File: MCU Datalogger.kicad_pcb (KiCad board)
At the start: 2 copper layers, 29 parts, among them J1 Conn_01x04_Pin, J2 Conn_01x09_Pin, J3 Conn_01x04_Pin, J4 Conn_02x03_Odd_Even, U1 DS1337S+, U2 24LC1025, U3 24LC1025, U4 ATMEGA328P-AU, Y1 32.768 KHz, Y2 16 MHz

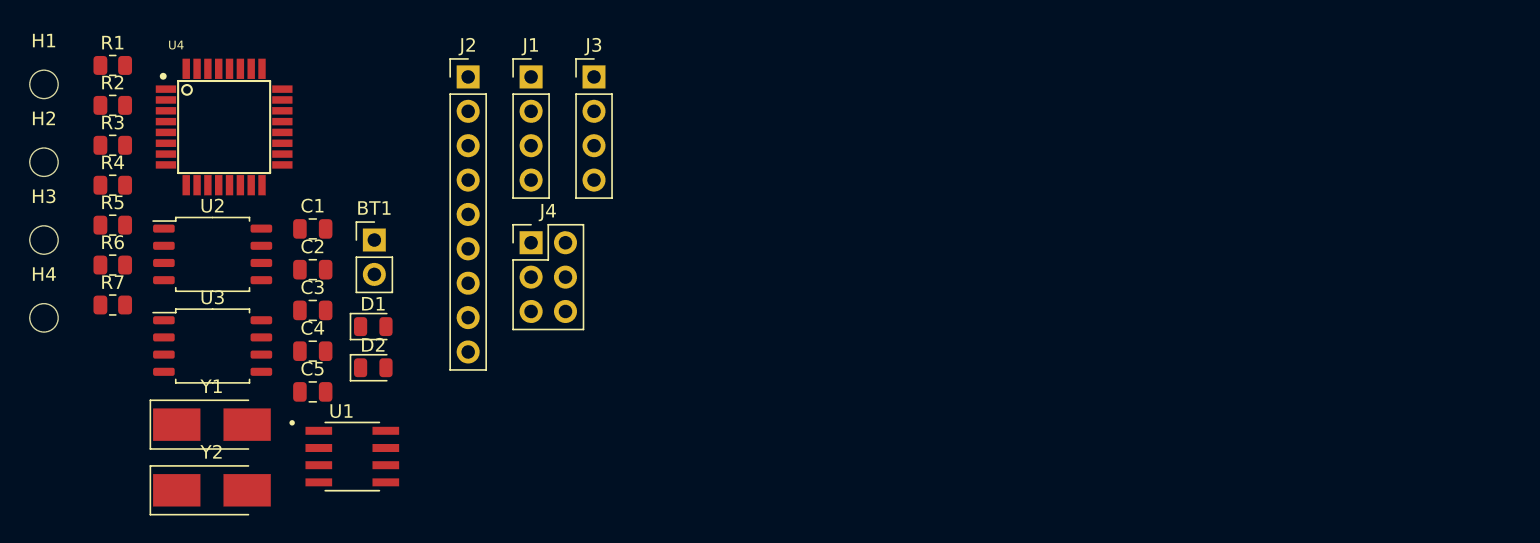
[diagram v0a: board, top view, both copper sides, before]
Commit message: Completed placement of footprints.
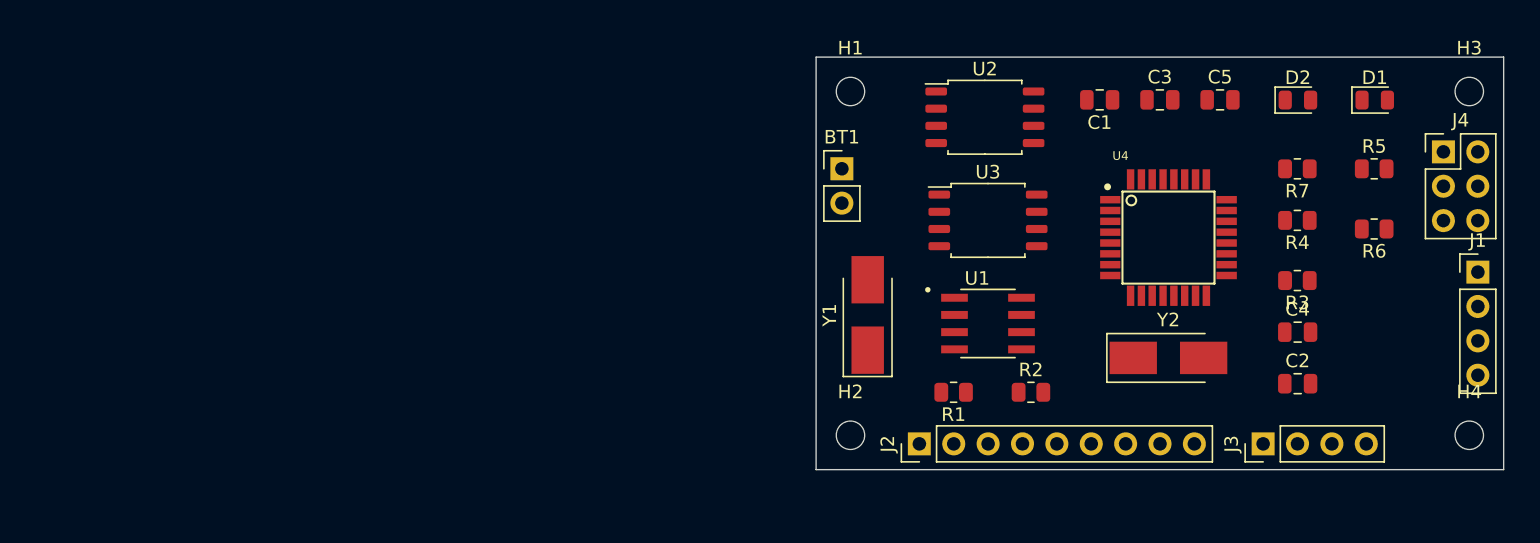
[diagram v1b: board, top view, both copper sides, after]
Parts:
- moved H3 105.9 mm to (165.7, 67.3)
- moved H4 105.7 mm to (165.7, 92.7)
- moved R5 93.3 mm to (158.7, 73.0)
- moved R6 93.2 mm to (158.7, 77.5), turned to 180 degrees
- moved R7 88.1 mm to (153.0, 73.0), turned to 180 degrees
- moved R3 88.1 mm to (153.0, 81.3), turned to 180 degrees
- moved R4 87.6 mm to (153.0, 76.8), turned to 180 degrees
- moved D1 75.9 mm to (158.8, 67.9)
- moved C2 73.3 mm to (153.1, 88.9)
- moved C4 72.8 mm to (153.1, 85.1)
- moved J1 71.4 mm to (166.4, 80.7)
- moved Y2 71.3 mm to (143.5, 87.0)
- moved D2 71.1 mm to (153.1, 67.9)
- moved R2 71.1 mm to (133.3, 89.5)
- moved C5 70.4 mm to (147.3, 67.9)
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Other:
- board outline added: 50.8 x 30.5 mm

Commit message: Refined and completed outline
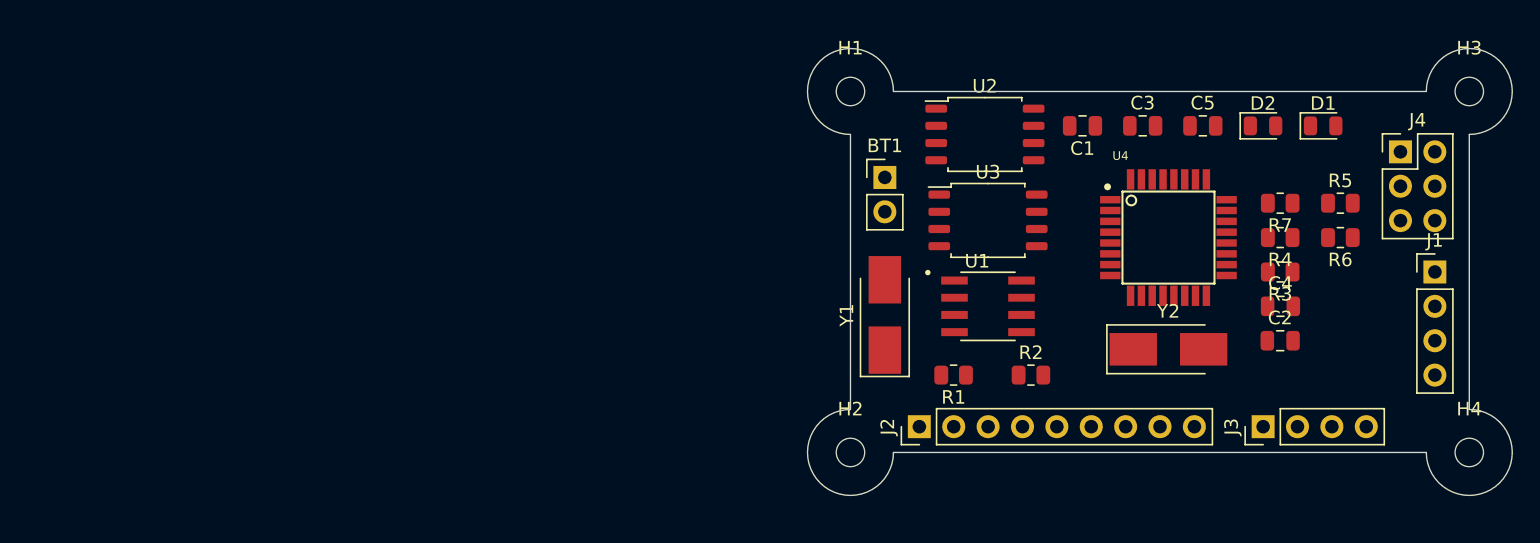
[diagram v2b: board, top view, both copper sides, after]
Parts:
- moved D1 4.26 mm to (154.9, 69.8)
- moved R5 3.56 mm to (156.2, 75.6)
- moved C2 3.43 mm to (151.8, 85.7)
- moved BT1 3.24 mm to (122.6, 73.7)
- moved D2 3.21 mm to (150.5, 69.8)
- moved J1 3.18 mm to (163.2, 80.6)
- moved J4 3.17 mm to (160.7, 71.8)
- moved R7 2.84 mm to (151.8, 75.6)
- moved R6 2.58 mm to (156.2, 78.1)
- moved C1 2.30 mm to (137.2, 69.8)
- moved C3 2.30 mm to (141.6, 69.8)
- moved C5 2.30 mm to (146.1, 69.8)
- moved C4 2.29 mm to (151.8, 83.2)
- moved R4 1.80 mm to (151.8, 78.1)
- moved R3 1.42 mm to (151.8, 80.6)
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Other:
- board size 50.8 x 30.5 mm -> 52.1 x 33 mm

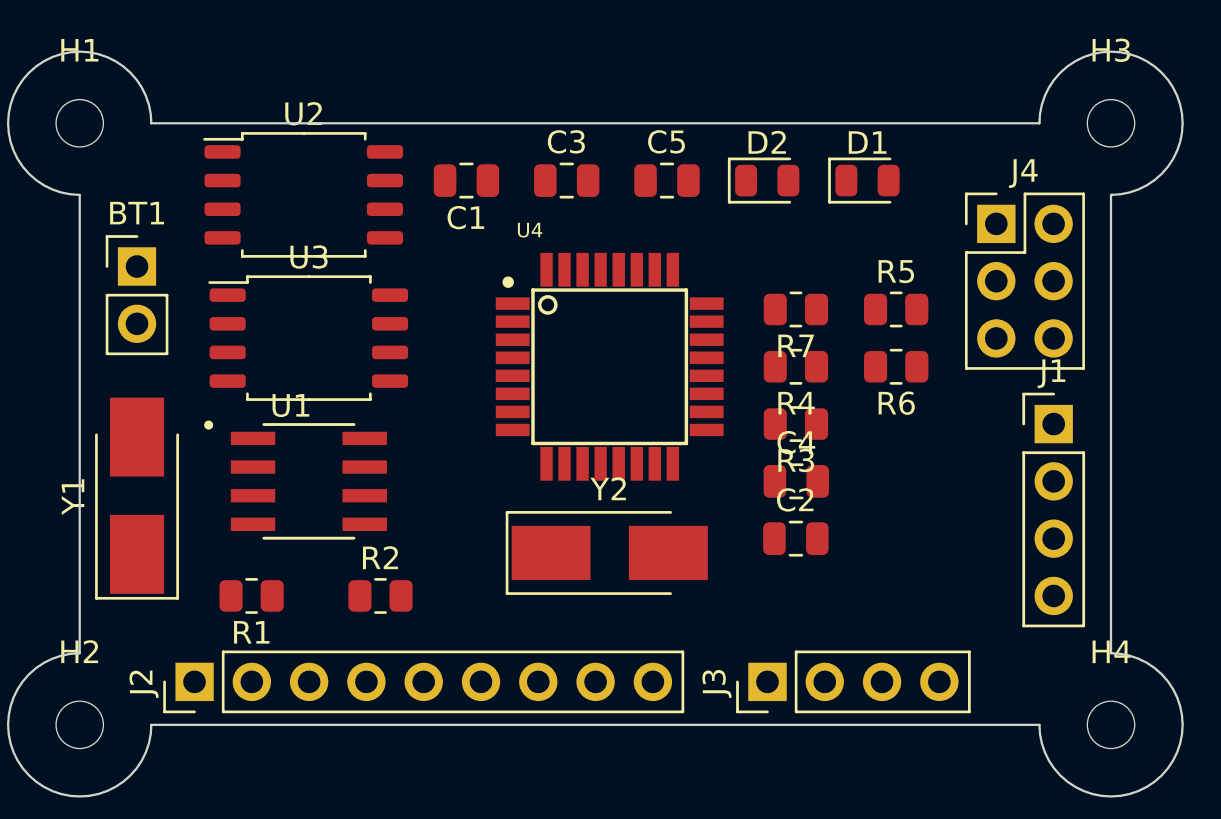
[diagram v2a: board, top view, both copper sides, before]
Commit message: Routing sans GND Vcc complete.
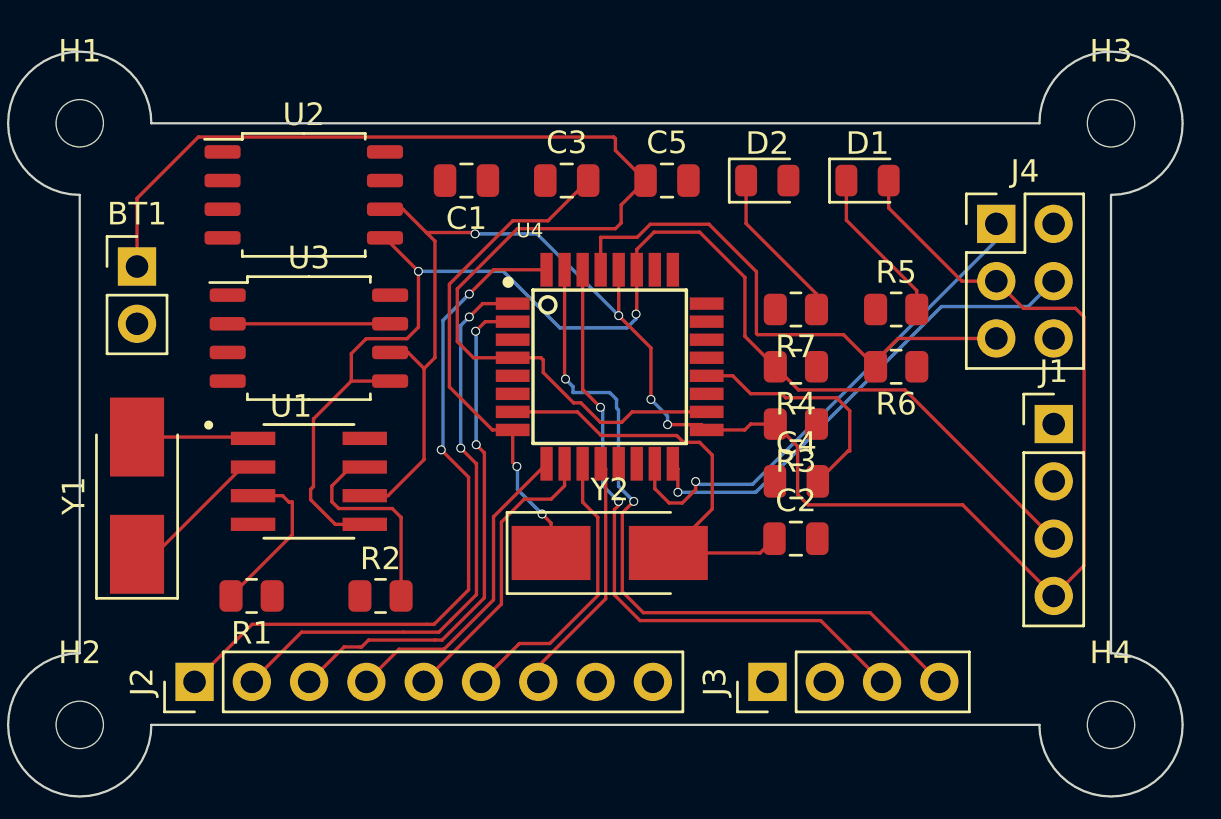
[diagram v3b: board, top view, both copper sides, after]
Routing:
- net /SCK: track 0.00 -> 82.8 mm, vias 0 -> 4
- net /SDA: track 0.00 -> 59.7 mm, vias 0 -> 2
- net Net-(BT1-+): track 0.00 -> 54.0 mm
- net /TX: track 0.00 -> 32.4 mm, vias 0 -> 2
- net /D2: track 0.00 -> 31.8 mm, vias 0 -> 2
- net /RX: track 0.00 -> 28.6 mm, vias 0 -> 2
- net /D3: track 0.00 -> 26.5 mm, vias 0 -> 2
- net /RESET: track 0.00 -> 24.1 mm
- net /D4: track 0.00 -> 23.1 mm, vias 0 -> 2
- net /MOSI: track 0.00 -> 22.4 mm, vias 0 -> 1
- net Net-(U4-PB7): track 0.00 -> 22.4 mm, vias 0 -> 2
- net /MISO: track 0.00 -> 21.9 mm, vias 0 -> 1
- net Net-(U4-PB6): track 0.00 -> 19.8 mm
- net /D5: track 0.00 -> 14.1 mm
- net /D6: track 0.00 -> 13.0 mm
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
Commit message: Completed wiring. Many improvements pending.
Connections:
- BT1 pad 1: Net-(BT1-+) -> /Vcc
- C5 pad 1: Net-(BT1-+) -> /Vcc
- D2 pad 2: Net-(BT1-+) -> /Vcc
- U4 pad 18: Net-(BT1-+) -> /Vcc
- U4 pad 4: Net-(BT1-+) -> /Vcc
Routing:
- net /Vcc: track 0.00 -> 97.7 mm, vias 0 -> 8
- net Net-(BT1-+): track 54.0 -> 0.00 mm
- net GND: track 0.00 -> 37.7 mm, vias 0 -> 10
- net Net-(U4-AREF): track 10.8 -> 12.5 mm
- net /TX: track 32.4 -> 31.5 mm
- net /SDA: track 59.7 -> 59.0 mm
- added copper zone on F.Cu, net /Vcc
- added copper zone on B.Cu, net GND

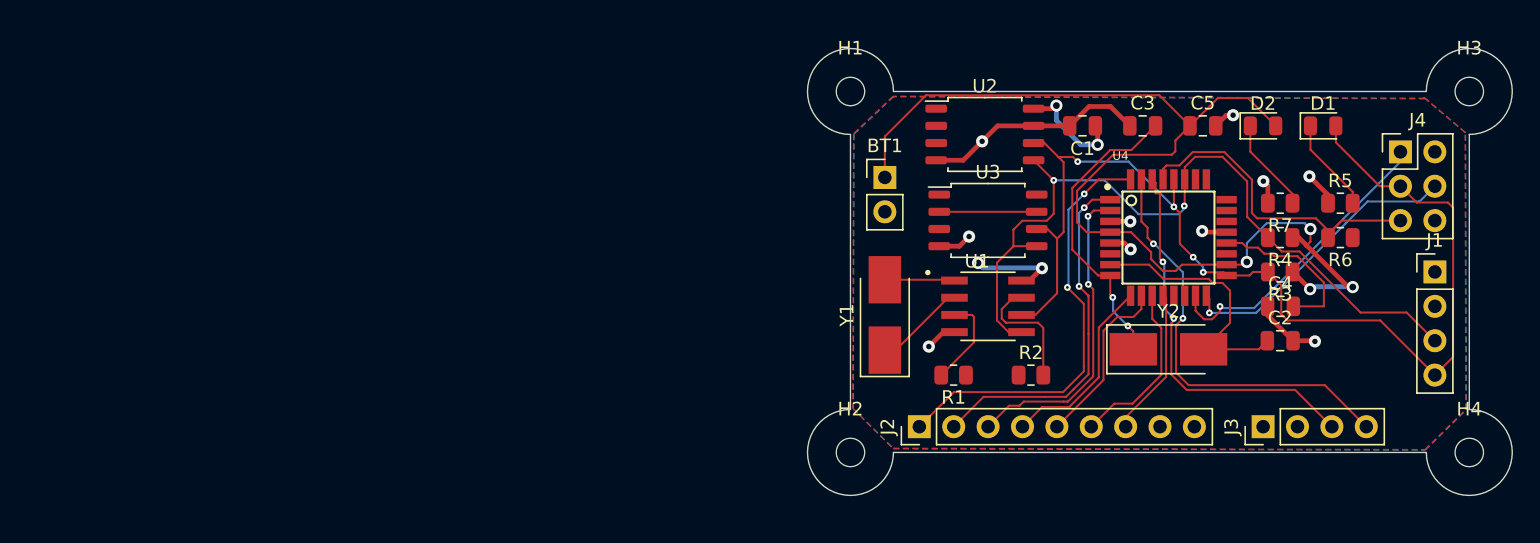
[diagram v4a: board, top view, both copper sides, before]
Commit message: Fixed all issues and warnings, and refined routing.
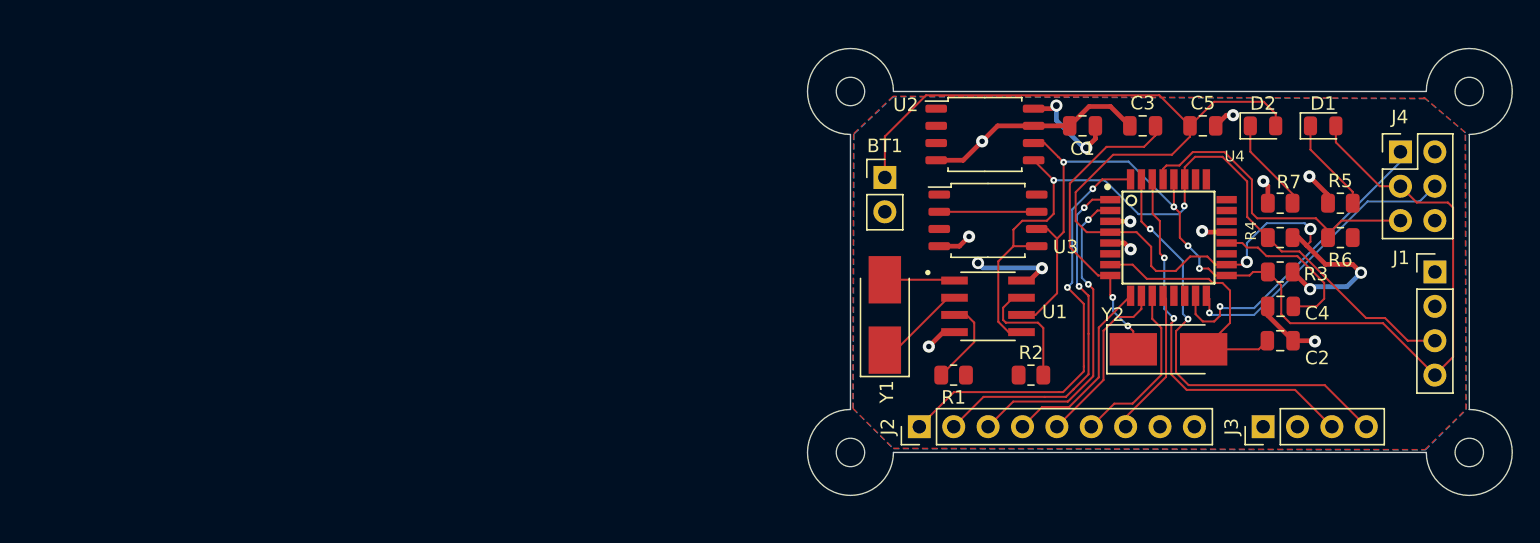
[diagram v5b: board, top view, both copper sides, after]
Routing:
- net /Vcc: track 97.7 -> 100.0 mm
- net Net-(U4-PB7): track 22.4 -> 23.2 mm
- net /SCK: track 82.8 -> 82.3 mm

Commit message: Ready to manufacture version 1.
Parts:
- added G***: LOGO, Footprints for project:TE_Logo_11.6x4, B.Cu at (152.0, 79.8)
- added REF**: KiCad-Logo2_5mm_SilkScreen, Symbol:KiCad-Logo2_5mm_SilkScreen, B.Cu at (151.5, 72.7)
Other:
- board text added: "2"
- board text added: "3"
- board text added: "4"
- board text added: "5"
- board text added: "6"
- board text added: "7"
- board text added: "8"
- board text added: "GN"
- board text added: "GND"
- board text added: "GPIO"
- board text added: "I2C"
- board text added: "ICSP"
- board text added: "MI"
- board text added: "MO"
- board text added: "RS"
- board text added: "Rx"
- board text added: "SC"
- board text added: "SCK"
- board text added: "SDA"
- board text added: "SERIAL"
- board text added: "Tx"
- board text added: "Vc"
- board text added: "Vcc"
